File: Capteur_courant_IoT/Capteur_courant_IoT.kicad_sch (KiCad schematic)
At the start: 6 parts, among them J2 Conn_01x04_Socket, J3 Screw_Terminal_01x02, J4 Conn_01x04_Socket, J5 USB4105-GF-A

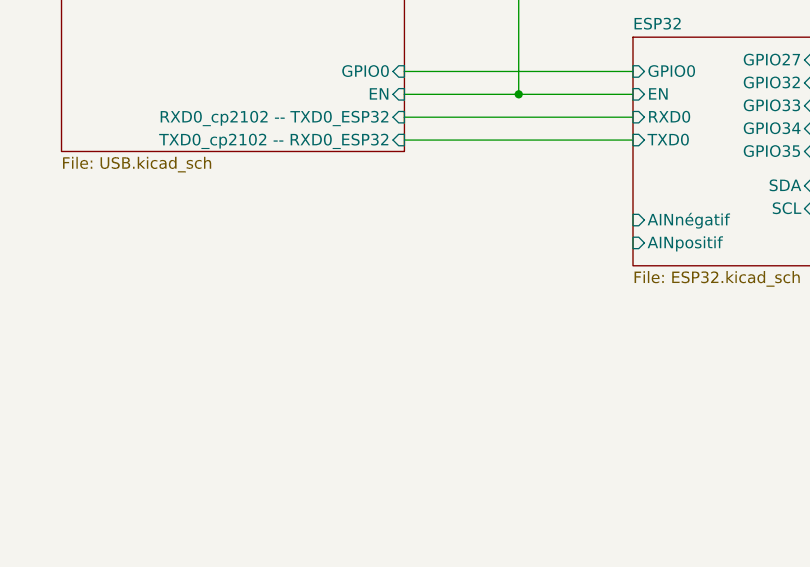
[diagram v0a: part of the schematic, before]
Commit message: ajout bornier pour capteur de courant
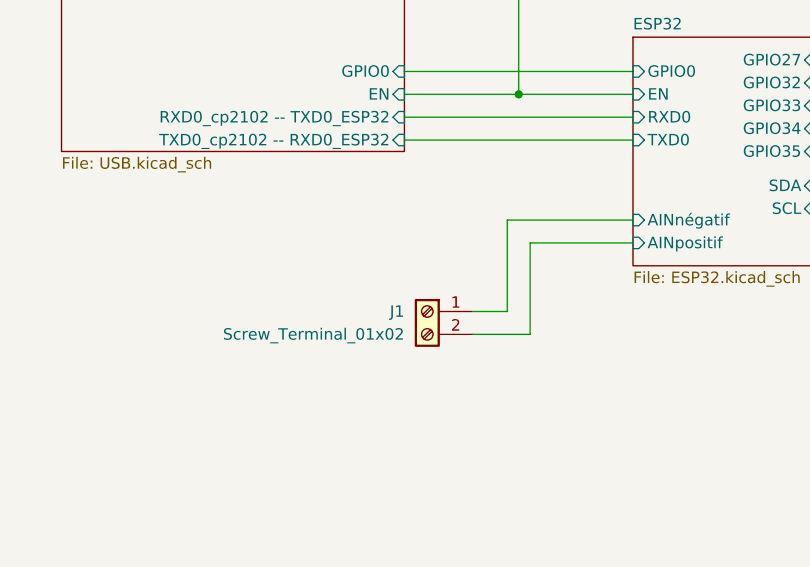
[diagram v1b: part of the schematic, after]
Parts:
- added J1: Screw_Terminal_01x02, symbol Connector:Screw_Terminal_01x02
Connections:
- net ESP32/AINnégatif: now also J1.1 (Pin_1)
- net ESP32/AINpositif: now also J1.2 (Pin_2)
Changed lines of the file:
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@@
+	(wire
+		(pts
+			(xy 138.43 106.68) (xy 138.43 96.52)
+		)
+		(stroke
+			(width 0)
+			(type default)
+		)
+	)
 	(wire
 		(pts
@@
 	(wire
 		(pts
+			(xy 140.97 109.22) (xy 134.62 109.22)
+		)
+		(stroke
+			(width 0)
+			(type default)
+		)
+	)
+	(wire
+		(pts
 			(xy 67.31 63.5) (xy 76.2 63.5)
 		)
@@
 	(wire
 		(pts
+			(xy 134.62 106.68) (xy 138.43 106.68)
+		)
+		(stroke
+			(width 0)
+			(type default)
+		)
+	)
+	(wire
+		(pts
 			(xy 139.7 38.1) (xy 209.55 38.1)
 		)
@@
 	(wire
 		(pts
+			(xy 140.97 99.06) (xy 140.97 109.22)
+		)
+		(stroke
+			(width 0)
+			(type default)
+		)
+	)
+	(wire
+		(pts
 			(xy 67.31 53.34) (xy 74.93 53.34)
 		)
@@
 	(wire
 		(pts
+			(xy 138.43 96.52) (xy 152.4 96.52)
+		)
+		(stroke
+			(width 0)
+			(type default)
+		)
+	)
+	(wire
+		(pts
 			(xy 127 80.01) (xy 152.4 80.01)
 		)
@@
 		(pts
 			(xy 248.92 114.3) (xy 248.92 120.65)
+		)
+		(stroke
+			(width 0)
+			(type default)
+		)
+	)
+	(wire
+		(pts
+			(xy 152.4 99.06) (xy 140.97 99.06)
 		)
 		(stroke
@@
 					(unit 1)
 				)
+			)
+		)
+	)
+	(symbol
+		(lib_id "Connector:Screw_Terminal_01x02")
+		(at 129.54 106.68 0)
+		(mirror y)
+		(unit 1)
+		(exclude_from_sim no)
+		(in_bom yes)
+		(on_board yes)
+		(dnp no)
+		(fields_autoplaced yes)
+		(property "Reference" "J1"
+			(at 127 106.6799 0)
+			(effects
+				(font
+					(size 1.27 1.27)
+				)
+				(justify left)
+			)
+		)
+		(property "Value" "Screw_Terminal_01x02"
+			(at 127 109.2199 0)
+			(effects
+				(font
+					(size 1.27 1.27)
+				)
+				(justify left)
+			)
+		)
+		(property "Footprint" ""
+			(at 129.54 106.68 0)
+			(effects
+				(font
+					(size 1.27 1.27)
+				)
+				(hide yes)
+			)
+		)
+		(property "Datasheet" "~"
+			(at 129.54 106.68 0)
+			(effects
+				(font
+					(size 1.27 1.27)
+				)
+				(hide yes)
+			)
+		)
+		(property "Description" "Generic screw terminal, single row, 01x02, script generated (kicad-library-utils/schlib/autogen/connector/)"
+			(at 129.54 106.68 0)
+			(effects
+				(font
+					(size 1.27 1.27)
+				)
+				(hide yes)
+			)
+		)
+		(pin "1"
+		)
+		(pin "2"
+		)
+		(instances
+			(project "Capteur_courant_IoT"
+				(path "/9ec92dd4-bf7f-4382-b228-27fa2b950a1e"
+					(reference "J1")
+					(unit 1)
+				)

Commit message: correction des points évoqués
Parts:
- removed D3, D7: SP0503BAHT, Package_TO_SOT_SMD:SOT-143, symbol Power_Protection:SP0503BAHT
- added D11: ESDZL5-1F4, Diode_SMD:D_0201_0603Metric, symbol Device:D
- added D12: ESDZL2012MX4T5G, Diode_SMD:D_0201_0603Metric, symbol Device:D
- added U6, U7: D3V3XA4B10LP, Package_DFN_QFN:Diodes_UDFN-10_1.0x2.5mm_P0.5mm, symbol Power_Protection:D3V3XA4B10LP
- J2, J4: footprint (none) -> Connector_PinHeader_2.54mm:PinHeader_1x04_P2.54mm_Vertical
- J5: footprint USB4105-GF-A:GCT_USB4105-GF-A -> Library_iot:GCT_USB4105-GF-A
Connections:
- net +3.3V: now also U6.4, U7.4
- net ESP32/AINpositif: now also D12.1 (K)
- net ESP32/SCL: now also U6.1, U7.1
- net ESP32/SDA: now also U6.2, U7.2
- net GND: now also D11.2 (A), D12.2 (A), U6.3 (VSS), U6.8 (VSS), U7.3 (VSS), U7.8 (VSS)
- net Vin: now also D11.1 (K)
- no-connect marks 4 -> 6
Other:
- moved on the sheet: J3, J4

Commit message: V100
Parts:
- removed J1, J3: Screw_Terminal_01x02, symbol Connector:Screw_Terminal_01x02
- added H1, H2, H3: MountingHole_Pad, MountingHole:MountingHole_3.2mm_M3_DIN965_Pad, symbol Mechanical:MountingHole_Pad
- added J1, J3: ED555/2DS, Library_iot:CONN_ED555&slash_2DS_OST, symbol library_perso:ED555_2DS
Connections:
- net +3.3V: now also J2.3 (Pin_3), J4.3 (Pin_3); no longer J2.4 (Pin_4), J4.4 (Pin_4)
- net ESP32/AINnégatif: now also J3.1
- net ESP32/AINpositif: now also J3.2
- net GND: now also J2.4 (Pin_4), J4.4 (Pin_4), H1.1, H2.1, H3.1, J1.1; no longer J2.3 (Pin_3), J4.3 (Pin_3)
- net Vin: now also J1.2
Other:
- sheet ESP32 ports: added RXD0_cp2102 -- TXD0_ESP32, TXD0_cp2102 -- RXD0_ESP32; removed RXD0, TXD0
